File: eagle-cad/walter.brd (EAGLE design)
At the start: 20.3 x 11.1 mm, 14 parts, among them U1 LP38511MRX-ADJ/NOPB

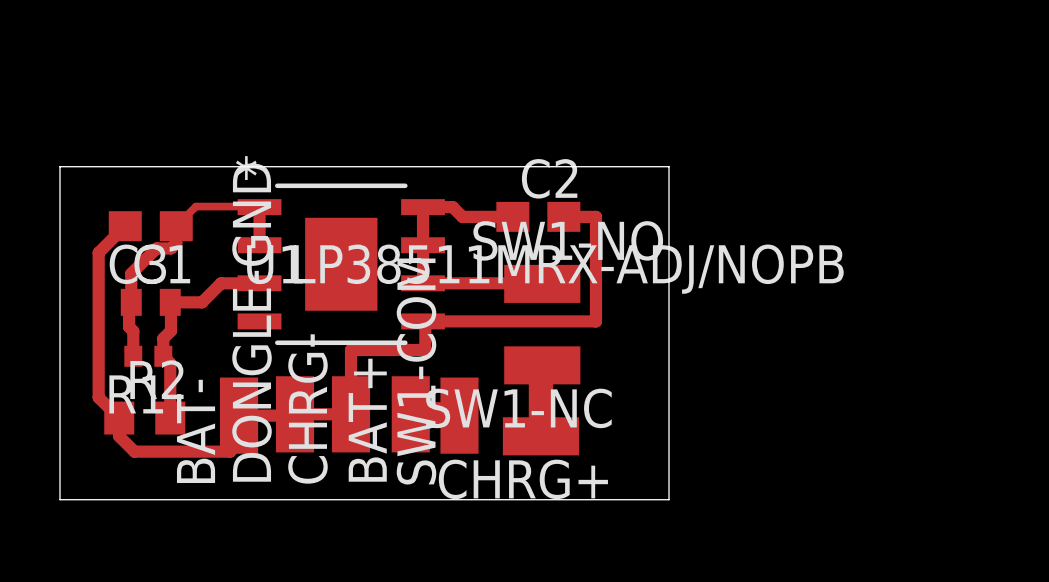
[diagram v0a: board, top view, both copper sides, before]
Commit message: schematics update
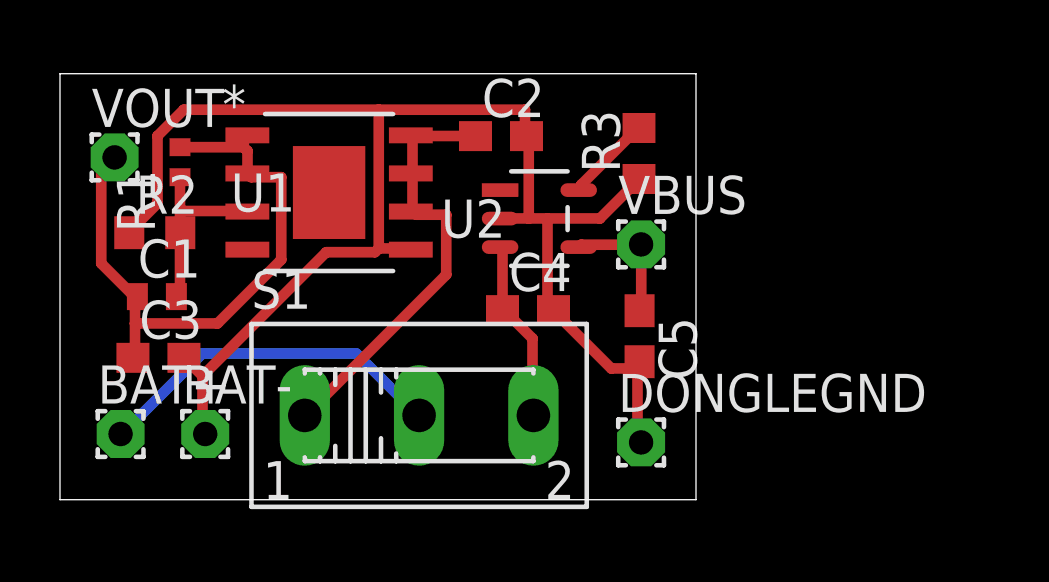
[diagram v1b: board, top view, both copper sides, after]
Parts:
- removed CHRG+, CHRG-, DONGLE-GND, SW1-COM, SW1-NC, SW1-NO: (no value), wirepad:SMD1,27-2,54
- added C4: 4.1uF, rcl:C0603
- added C5: 4.6uF, rcl:C0603
- added DONGLEGND, VBUS, VOUT: (no value), wirepad:1,6/0,8
- added R3: 2.2K, rcl:R0603
- added S1: (no value), switch:255SB
- added U2: LTC4054LES5-4.2TRPBF, LTC4054:S_5_ADI
- BAT+, BAT-: device wirepad:SMD1,27-2,54 -> wirepad:1,6/0,8
- moved BAT+ 9.70 mm to (2.02, 2.19)
- moved R1 6.56 mm to (4.00, 11.2), turned to 90 degrees
- moved R2 6.19 mm to (3.16, 8.90)
- moved C3 4.40 mm to (3.28, 4.73), turned to 0 degrees
- moved C2 2.97 mm to (14.7, 12.1)
- moved U1 2.43 mm to (8.97, 10.2)
- moved BAT- 1.28 mm to (4.84, 2.19)
- moved C1 0.28 mm to (3.23, 6.77)
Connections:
- new net N$2: C4.1, S1.3, U2.3
- new net N$6: R3.2, U2.5
- net GND: now also C4.2, C5.2, DONGLEGND.1, R3.1, U2.2; no longer CHRG-.1, DONGLE-GND.1
- net N$1: now also S1.1; no longer SW1-NO.1
- net N$3: now also VOUT.1
- net N$5: now also S1.2; no longer SW1-COM.1
- net N$7: now also C5.1, U2.4, VBUS.1; no longer CHRG+.1, SW1-NC.1
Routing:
- net GND: track 32.6 -> 51.0 mm
- net N$3: track 9.65 -> 20.8 mm
- net N$5: track 1.64 -> 11.9 mm
- net N$2: track 0.00 -> 6.10 mm
- net N$1: track 9.65 -> 14.7 mm
- net N$6: track 0.00 -> 2.93 mm
- net N$7: track 2.38 -> 4.34 mm
- net N$4: track 7.31 -> 6.28 mm
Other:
- board size 20.3 x 11.1 mm -> 21.2 x 14.2 mm
